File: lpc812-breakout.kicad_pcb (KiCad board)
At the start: 2 copper layers, 0 parts

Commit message: Assign footprints, create net, place components on pcb
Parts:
- added C1: 0.1uF, local_footprints:0805_HS, F.Cu at (138.4, 97.4)
- added J1: Conn_01x10, local_footprints:Pin_Header_Straight_1x10_Pitch2.54mm, F.Cu at (127.0, 114.3)
- added J2: Conn_01x10, local_footprints:Pin_Header_Straight_1x10_Pitch2.54mm, F.Cu at (149.9, 94.0)
- added R1: R, local_footprints:1206_HS, F.Cu at (146.7, 104.1)
- added R2: R, local_footprints:1206_HS, F.Cu at (130.2, 104.1)
- added SW1: RESET, local_footprints:SW_SPST_PUSH_6mm_3mm, F.Cu at (149.9, 104.1)
- added SW2: ISP, local_footprints:SW_SPST_PUSH_6mm_3mm, F.Cu at (127.0, 104.1)
- added U1: LPC812M101JD20, local_footprints:SOIC-20W_7.5x12.8mm_Pitch1.27mm_HS, F.Cu at (138.4, 105.2)

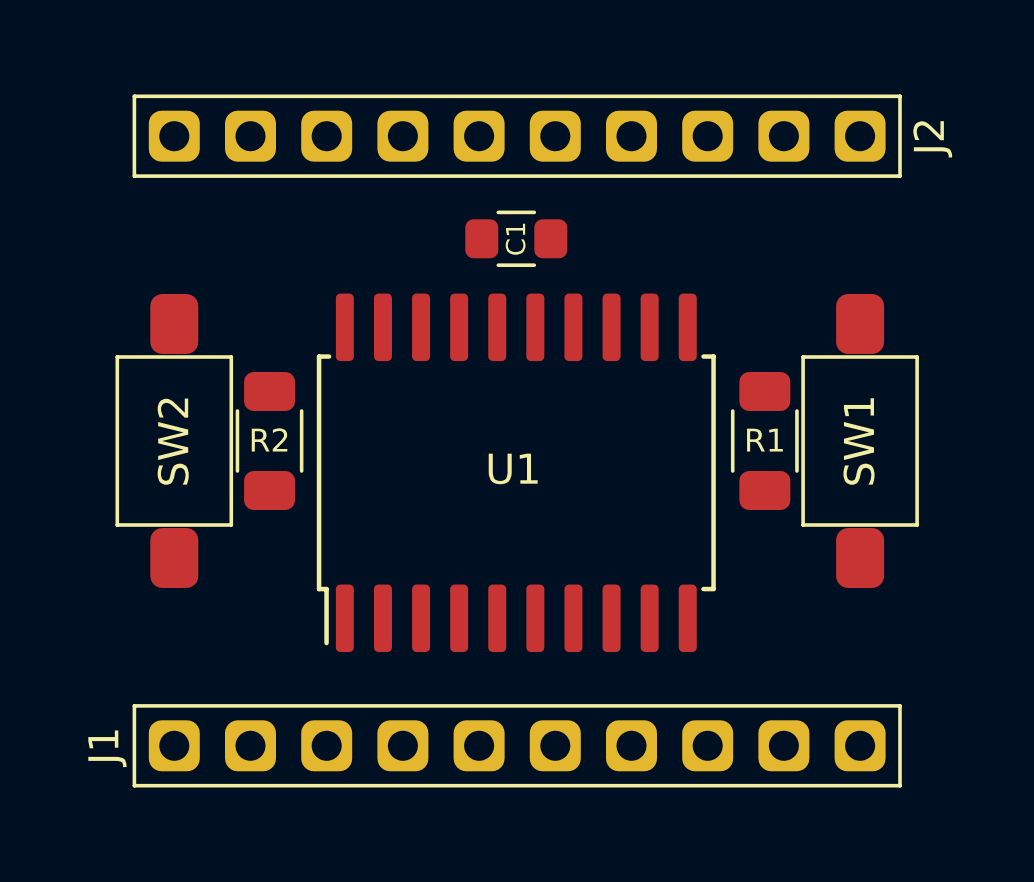
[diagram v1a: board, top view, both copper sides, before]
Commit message: Complete routing and silkscreen
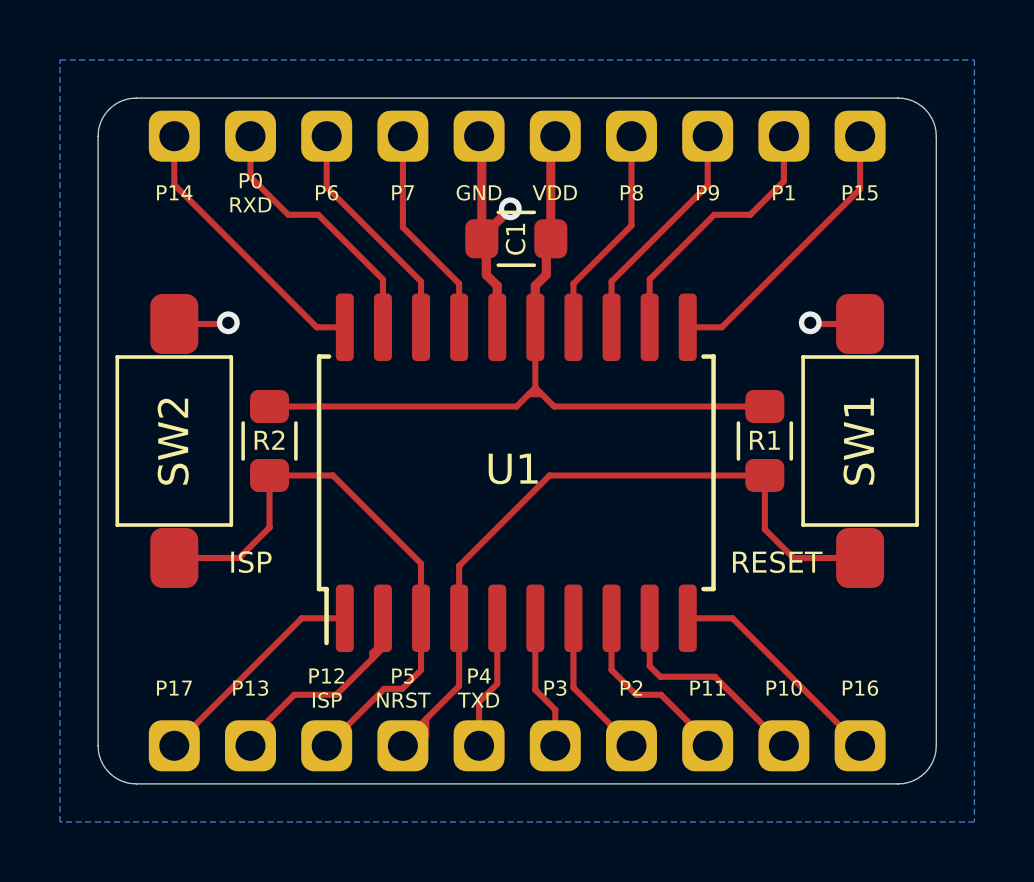
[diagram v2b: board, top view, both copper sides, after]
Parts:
- added REF***: OSHW-Logo_5.7x6mm_SilkScreen, Symbols:OSHW-Logo_5.7x6mm_SilkScreen, B.Cu at (145.5, 105.2)
- J1, J2: footprint local_footprints:Pin_Header_Straight_1x10_Pitch2.54mm -> local_footprints:Pin_Header_Straight_1x10_Pitch2.54mm_NoSilk
- R1, R2: footprint local_footprints:1206_HS -> local_footprints:0805_HS
- turned R2 to 270 degrees
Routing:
- net VDD: track 0.00 -> 26.1 mm
- net PIO_5.NRST: track 0.00 -> 24.2 mm
- net PIO_12.ISP: track 0.00 -> 19.3 mm
- net GND: track 0.00 -> 11.5 mm, vias 0 -> 3
- net PIO_15: track 0.00 -> 9.41 mm
- net PIO_14: track 0.00 -> 9.27 mm
- net PIO_1: track 0.00 -> 8.93 mm
- net PIO_0.RX: track 0.00 -> 8.78 mm
- net PIO_9: track 0.00 -> 7.70 mm
- net PIO_6: track 0.00 -> 7.67 mm
- net PIO_16: track 0.00 -> 7.51 mm
- net PIO_17: track 0.00 -> 7.45 mm
- net PIO_8: track 0.00 -> 7.17 mm
- net PIO_10: track 0.00 -> 7.17 mm
- net PIO_7: track 0.00 -> 7.15 mm
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- added copper zone on B.Cu, net GND
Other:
- board outline added: 27.9 x 22.9 mm
- rule pad_to_mask_clearance: 0.051 -> 0.0254
- rule solder_mask_min_width: 0.25 -> 0.1016
- board text added: "(C) Vlad Belous CC BY-SA 4.0 github.com/vladbelous/lpc812-breakout"
- board text added: "Flash: 16KB RAM: 4KB Cortex-M0+"
- board text added: "GND"
- board text added: "ISP"
- board text added: "NOTES:"
- board text added: "P0 RXD"
- board text added: "P1"
- board text added: "P10"
- board text added: "P11"
- board text added: "P12 ISP"
- board text added: "P13"
- board text added: "P14"
- board text added: "P15"
- board text added: "P16"
- board text added: "P17"
- board text added: "P2"
- board text added: "P3"
- board text added: "P4 TXD"
- board text added: "P5 NRST"
- board text added: "P6"
- board text added: "P7"
- board text added: "P8"
- board text added: "P9"
- board text added: "RESET"
- board text added: "Simple breakout for LPC812M101JD20FP VIN: 1.8 ~~ 3.6V"
- board text added: "VDD"
